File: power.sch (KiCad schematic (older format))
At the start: 36 parts, among them J201 USB_B_Micro, J202 LiPo, Q201 MBT3904DW1, Q203 2.5A/30V, SW201 SW_DIP_x01, SW202 SW_DIP_x01, U201 MCP73831, U202 FT231XS, U203 AP2112K-3.3

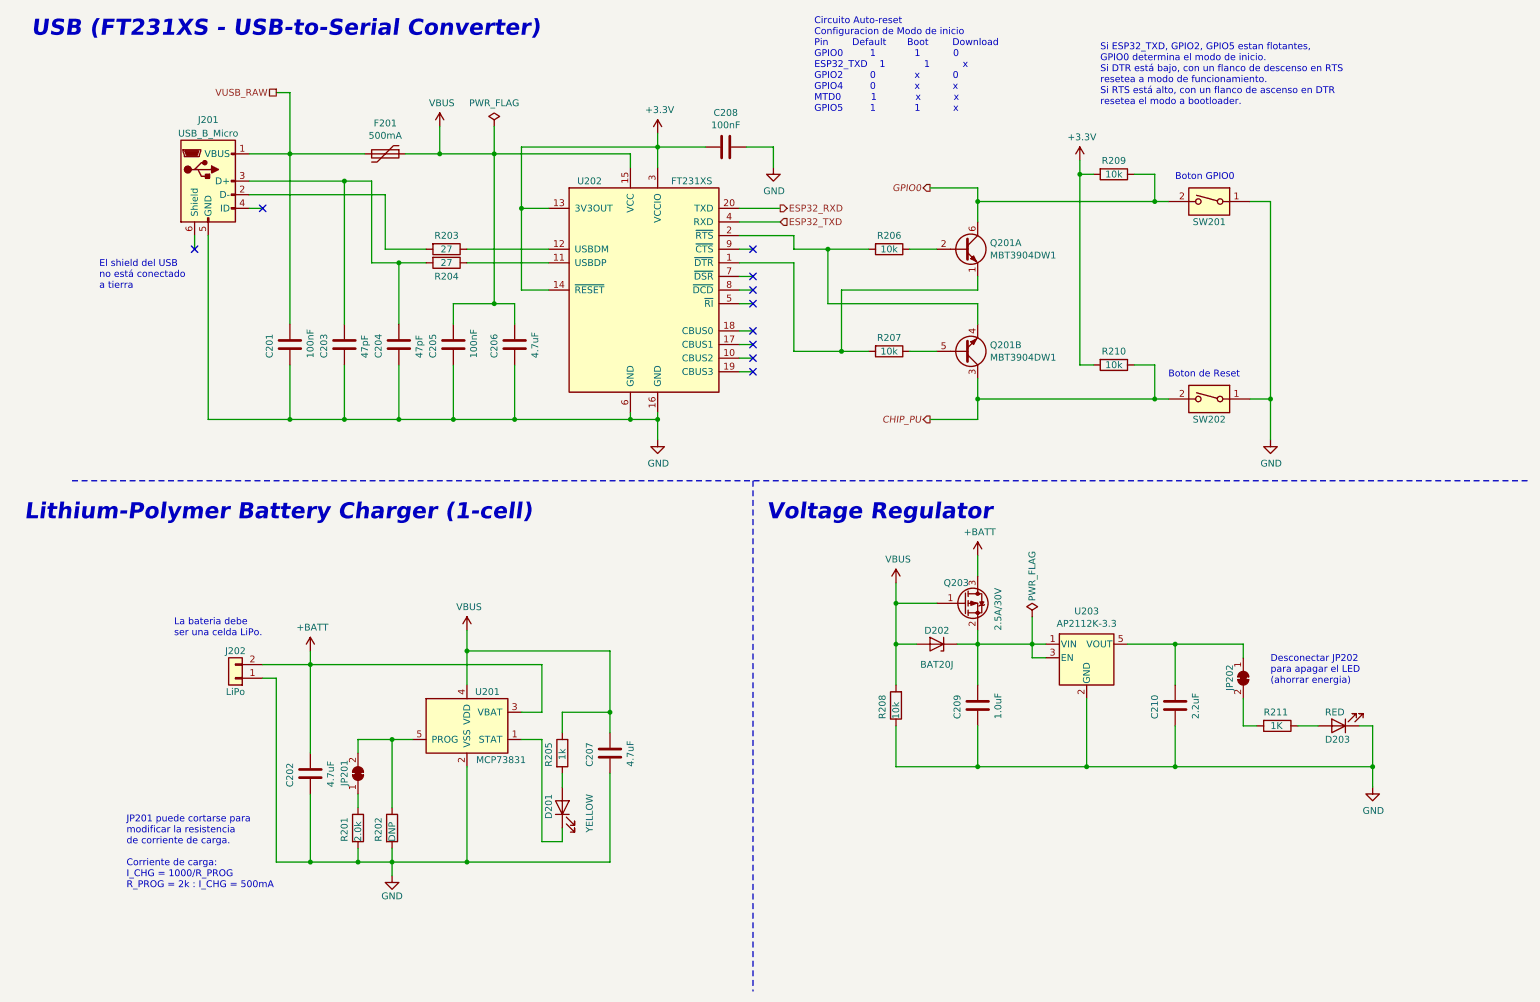
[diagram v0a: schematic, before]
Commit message: PMD03 - Creacion PCB y modelo 3D
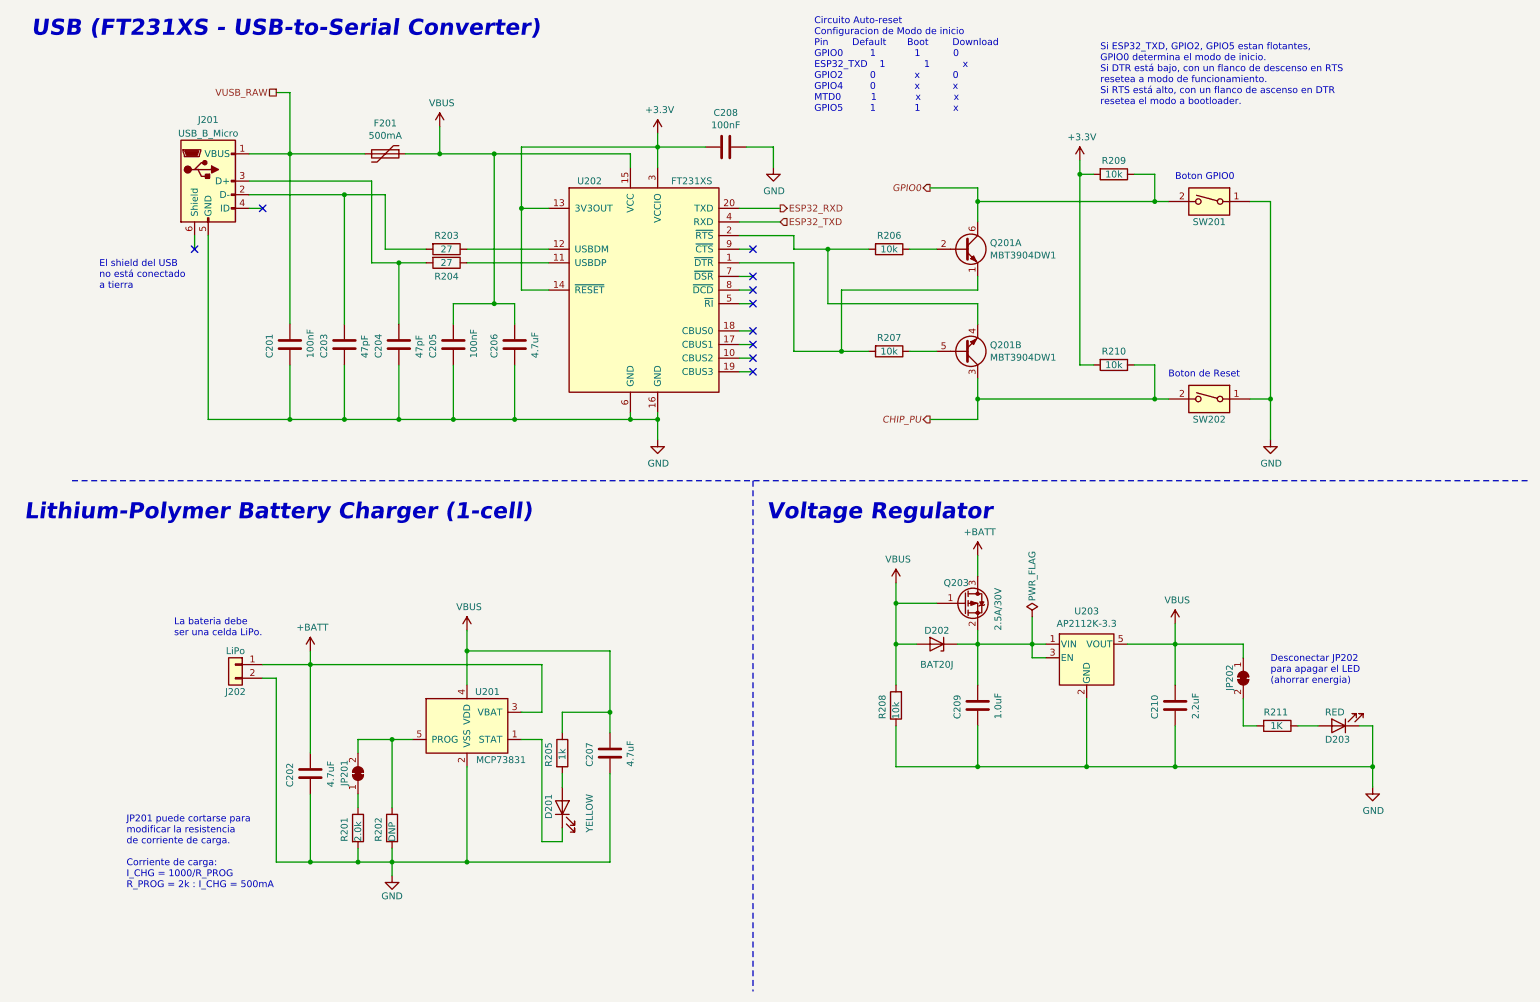
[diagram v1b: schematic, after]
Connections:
- net +BATT: now also J202.1 (Pin_1); no longer J202.2 (Pin_2)
- net GND: now also J202.2 (Pin_2); no longer J202.1 (Pin_1)
- net VBUS: now also C210.1, JP202.1 (A), U203.5 (VOUT)
- net at J201.2 (D-), R203.2: now also C203.1
- net at C204.1, J201.3 (D+), R204.2: no longer C203.1
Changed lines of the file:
@@
 	3250 2350 3250 1950
 Wire Wire Line
-	3250 1950 2250 1950
+	3250 1950 2950 1950
 Wire Wire Line
 	3550 2450 3350 2450
 Wire Wire Line
 	3150 2450 3150 1850
-Wire Wire Line
-	2250 1850 2950 1850
 Connection ~ 3350 2450
 Wire Wire Line
 	3350 2450 3150 2450
-Connection ~ 2950 1850
-Wire Wire Line
-	2950 1850 3150 1850
 $Comp
 L Device:C C205
@@
 Wire Wire Line
 	3350 2450 3350 2900
-Wire Wire Line
-	2950 1850 2950 2900
 Wire Wire Line
 	2550 1650 2550 2900
@@
 Circuito Auto-reset\nConfiguracion de Modo de inicio\nPin        Default       Boot        Download\nGPIO0         1             1           0\nESP32_TXD    1             1           x                \nGPIO2         0             x           0\nGPIO4         0             x           x\nMTD0          1             x           x\nGPIO5         1             1           x\n
 $Comp
-L Connector_Generic:Conn_01x02 J202
-U 1 1 5D256BBC
-P 2150 5500
-F 0 "J202" H 2150 5300 50  0000 C CNN
-F 1 "LiPo" H 2150 5600 50  0000 C CNN
-F 2 "Connector_JST:JST_PH_S2B-PH-K_1x02_P2.00mm_Horizontal" H 2150 5500 50  0001 C CNN
-F 3 "~" H 2150 5500 50  0001 C CNN
-	1    2150 5500
-	-1   0    0    1
-$EndComp
-$Comp
 L power:GND #PWR0203
 U 1 1 5D25E588
@@
 Connection ~ 3050 6850
 Wire Wire Line
-	2350 5500 2450 5500
-Wire Wire Line
-	2450 5500 2450 6850
-Wire Wire Line
-	2350 5400 2700 5400
-Wire Wire Line
 	2450 6850 2700 6850
 Wire Wire Line
@@
 Wire Wire Line
 	2550 1650 3100 1650
-$Comp
-L power:PWR_FLAG #FLG0101
-U 1 1 5DADC7B6
-P 4050 1450
-F 0 "#FLG0101" H 4050 1525 50  0001 C CNN
-F 1 "PWR_FLAG" H 4050 1623 50  0000 C CNN
-F 2 "" H 4050 1450 50  0001 C CNN
-F 3 "~" H 4050 1450 50  0001 C CNN
-	1    4050 1450
-	1    0    0    -1
-$EndComp
-Wire Wire Line
-	4050 1650 4050 1450
 Text Notes 1150 2650 0    50   ~ 0
 El shield del USB\nno está conectado \na tierra
@@
 	7000 4950 7000 4800
 Connection ~ 7000 4950
+$Comp
+L power:VBUS #PWR0118
+U 1 1 5D2CA312
+P 9050 5100
+F 0 "#PWR0118" H 9050 4950 50  0001 C CNN
+F 1 "VBUS" H 9065 5273 50  0000 C CNN
+F 2 "" H 9050 5100 50  0001 C CNN
+F 3 "" H 9050 5100 50  0001 C CNN
+	1    9050 5100
+	1    0    0    -1
+$EndComp
+Wire Wire Line
+	9050 5100 9050 5250
+$Comp
+L Connector_Generic:Conn_01x02 J202
+U 1 1 5D256BBC
+P 2150 5400
+F 0 "J202" H 2150 5200 50  0000 C CNN
+F 1 "LiPo" H 2150 5500 50  0000 C CNN
+F 2 "Connector_JST:JST_PH_S2B-PH-K_1x02_P2.00mm_Horizontal" H 2150 5400 50  0001 C CNN
+F 3 "~" H 2150 5400 50  0001 C CNN
+	1    2150 5400
+	-1   0    0    -1
+$EndComp
+Wire Wire Line
+	2450 5500 2450 6850
+Wire Wire Line
+	2450 5500 2350 5500
+Wire Wire Line
+	2350 5400 2700 5400
+Wire Wire Line
+	2250 1850 3150 1850
+Wire Wire Line
+	2950 2900 2950 1950
+Connection ~ 2950 1950
+Wire Wire Line
+	2950 1950 2250 1950
 $EndSCHEMATC

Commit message: Correcciones
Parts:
- J201: footprint Connector_USB:USB_Micro-B_Wuerth_629105150521 -> Connector_USB:USB_Micro-B_GCT_USB3076-30-A
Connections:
- net GND: now also J201.6 (Shield)
- net VBUS: now also R205.2; no longer R205.1
- net at D201.2 (A): now also R205.1; no longer R205.2
- no-connect marks 10 -> 9
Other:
- note added: "Manufacturer Diodes Incorporated \nMfr. Part # AP2112K-3.3TRG1 \nMouser Part # 621-AP2112K-3.3TRG1 \nPackage # SOT-25-5"
- note added: "Manufacturer FTDI\nMfr. Part # FT231XS-R\nMouser Part # 895-FT231XS-R\nPackage # SSOP-20"
- note added: "Manufacturer Microchip Technology \nMfr. Part # MCP73831T-2ACI/OT \nMouser Part # 579-MCP73831T-2ACIOT \nPackage # SOT-23"
- note removed: "El shield del USB\nno está conectado \na tierra"
- moved on the sheet: C202, C207, D201, J202, JP201, R201, R202, R205, U201
